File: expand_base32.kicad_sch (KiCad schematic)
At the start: 141 parts, among them J1 Vin, J10 LED_9, J11 LED_10, J12 H_5V, J13 S_5V, J14 H_3V3, J15 H_SERVO, J16 S_3V3, J17 BUZZER, J18 H_GND, J19 S_GND, J2 LED_1, J20 DIP_01, J21 INPUT DIP, J22 DIP_02, J23 LED_10, J24 LED_10, J25 DIP_01, J26 DIP_01, J27 INPUT_LM35, J28 POT_01, J29 POT_02, J3 LED_2, J30 LED_10, J31 INPUT_DS18B20, J32 LED_10, J33 LDR_01, J34 LED_10, J35 LED_10, J36 POT_02, J37 LED_10, J38 LED_10, J39 DIP_01, J4 LED_3, J40 DIP_01, J41 INPUT_BTN, J42 M1, J43 M2, J44 MOTOR SRC, J45 EN_1, J46 EN_2, J47 IN_M1A, J48 IN_M1B, J49 IN_M2A, J5 LED_4, J50 IN_M2B, J6 LED_5, J7 LED_6, J8 LED_7, J9 LED_8, M1 Servo, M2 Motor_DC, M3 Motor_DC, M4 MOTOR PAP, SW1 SW_DIP_x10, SW2 INPUT_D1, SW3 INPUT_D2, SW4 INPUT_D1, SW5 INPUT_D1, SW6 INPUT_D2, SW7 INPUT_D2, SW8 INPUT_D1, SW9 INPUT_D2, U1 LM7805_TO220, U2 L293D, U3 AMS1117, U4 ULN2003A, U6 DS18B20, U7 LM35-LP

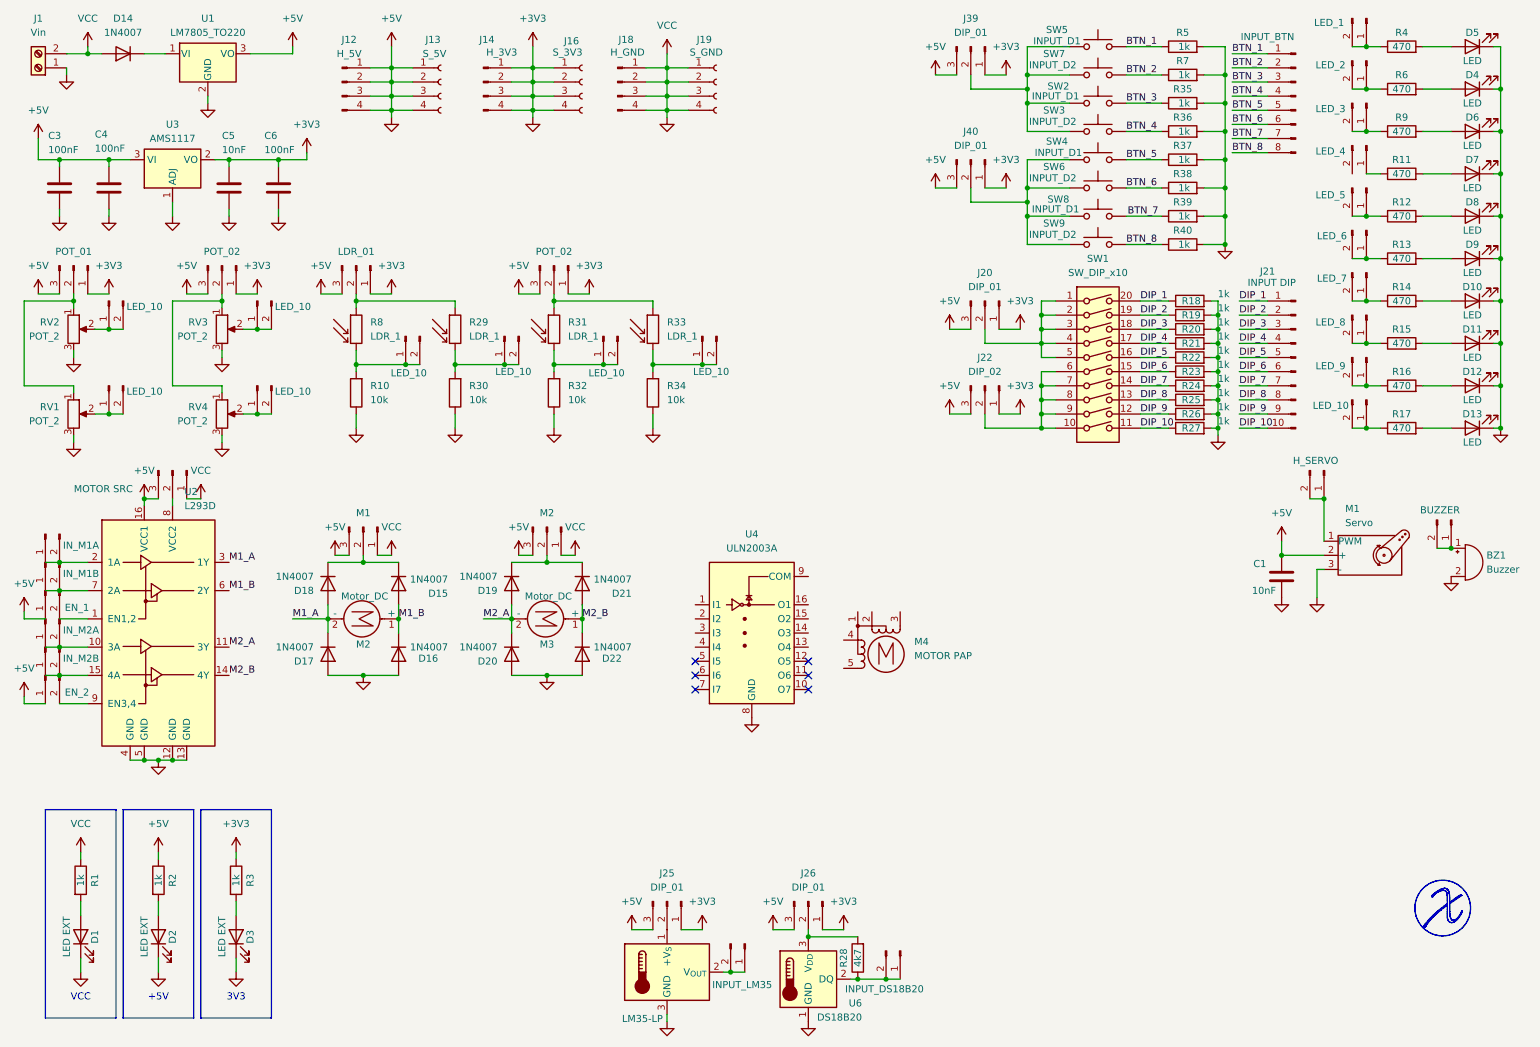
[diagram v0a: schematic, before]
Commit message: add: more components
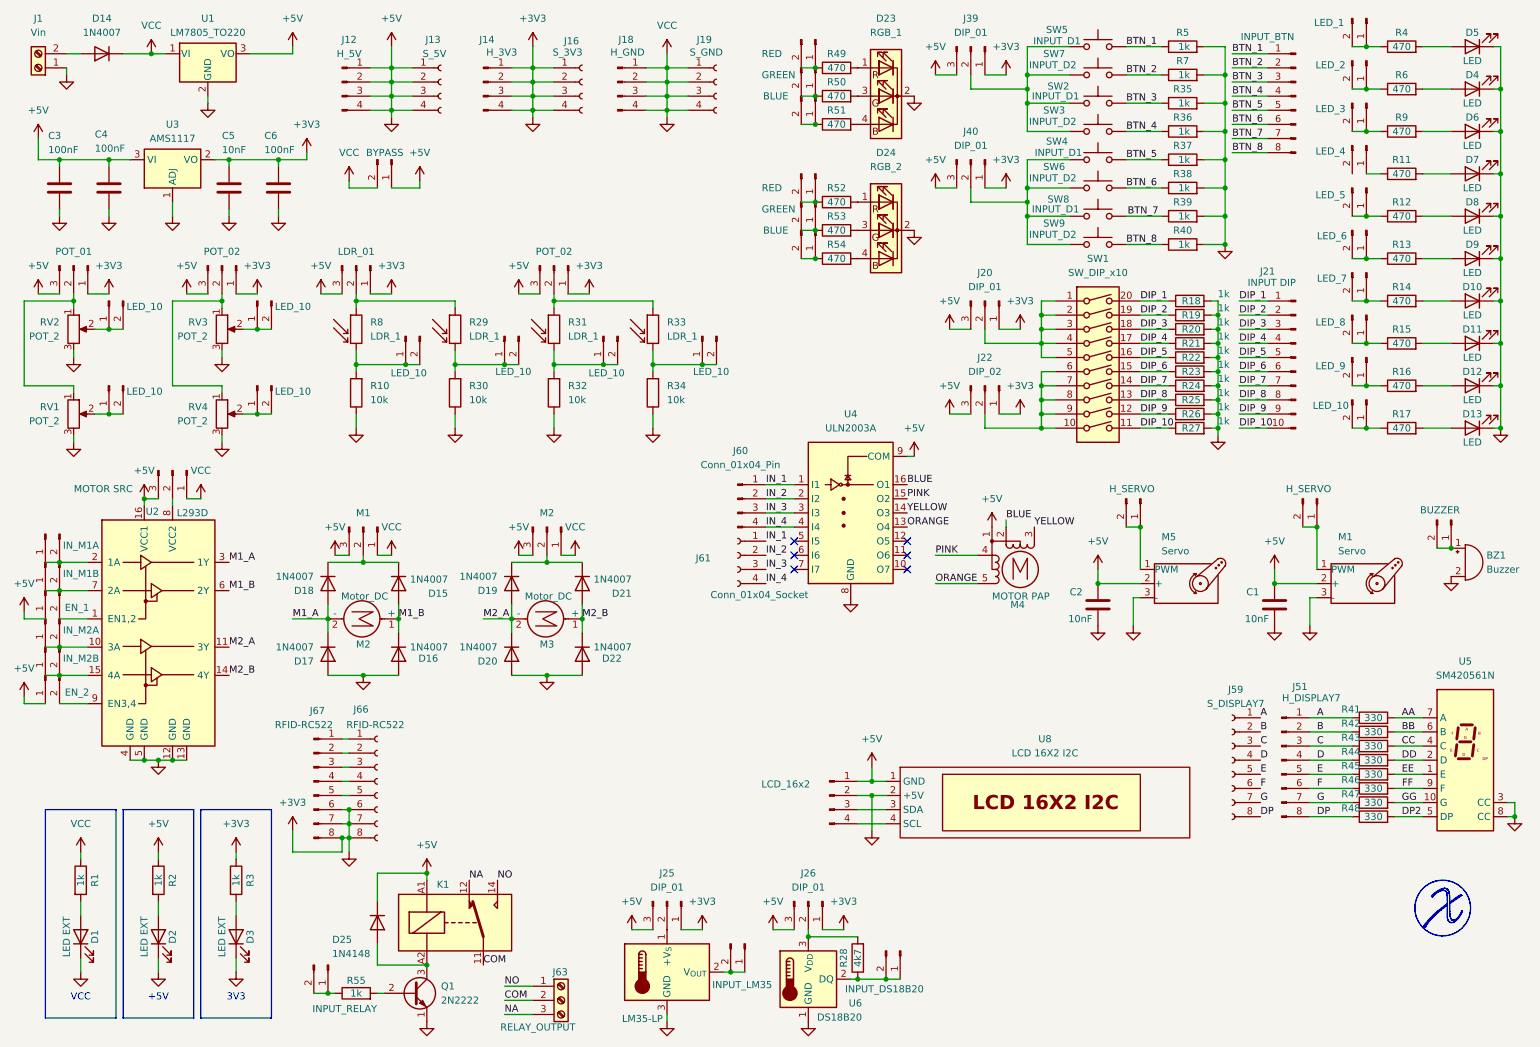
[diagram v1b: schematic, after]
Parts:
- added C2: 10nF, Capacitor_SMD:C_0805_2012Metric, symbol Device:C
- added D23: RGB_1, symbol Device:LED_RKGB
- added D24: RGB_2, symbol Device:LED_RKGB
- added D25: 1N4148, Diode_THT:D_DO-35_SOD27_P7.62mm_Horizontal, symbol Diode:1N4148
- added J51: H_DISPLAY7, Connector_PinHeader_2.54mm:PinHeader_1x08_P2.54mm_Vertical, symbol Connector:Conn_01x08_Pin
- added J52, J56: RED, Connector_PinHeader_2.54mm:PinHeader_1x02_P2.54mm_Vertical, symbol Connector:Conn_01x02_Pin
- added J53: BYPASS, Connector_PinHeader_2.54mm:PinHeader_1x02_P2.54mm_Vertical, symbol Connector:Conn_01x02_Pin
- added J54, J57: GREEN, Connector_PinHeader_2.54mm:PinHeader_1x02_P2.54mm_Vertical, symbol Connector:Conn_01x02_Pin
- added J55, J58: BLUE, Connector_PinHeader_2.54mm:PinHeader_1x02_P2.54mm_Vertical, symbol Connector:Conn_01x02_Pin
- added J59: S_DISPLAY7, symbol Connector:Conn_01x08_Socket
- added J60: Conn_01x04_Pin, symbol Connector:Conn_01x04_Pin
- added J61: Conn_01x04_Socket, symbol Connector:Conn_01x04_Socket
- added J62: H_SERVO, Connector_PinHeader_2.54mm:PinHeader_1x02_P2.54mm_Vertical, symbol Connector:Conn_01x02_Pin
- added J63: RELAY_OUTPUT, symbol Connector:Screw_Terminal_01x03
- added J64: LCD_16x2, symbol Connector:Conn_01x04_Pin
- added J65: INPUT_RELAY, Connector_PinHeader_2.54mm:PinHeader_1x02_P2.54mm_Vertical, symbol Connector:Conn_01x02_Pin
- added J66: RFID-RC522, symbol Connector:Conn_01x08_Socket
- added J67: RFID-RC522, symbol Connector:Conn_01x08_Pin
- added K1: JQC-3FF-005-1Z, Relay_THT:Relay_SPDT_Hongfa_JQC-3FF_0XX-1Z, symbol Relay:JQC-3FF-005-1Z
- added M5: Servo, Connector_PinHeader_2.54mm:PinHeader_1x03_P2.54mm_Vertical, symbol Motor:Motor_Servo_Futaba_J
- added Q1: 2N2222, Package_TO_SOT_THT:TO-92_Inline, symbol Transistor_BJT:PN2222A
- added R41, R42, R43, R44, R45, R46, R47, R48: 330, Resistor_THT:R_Axial_DIN0309_L9.0mm_D3.2mm_P12.70mm_Horizontal, symbol Device:R
- added R49, R50, R51, R52, R53, R54: 470, Resistor_THT:R_Axial_DIN0207_L6.3mm_D2.5mm_P10.16mm_Horizontal, symbol Device:R
- added R55: 1k, Resistor_THT:R_Axial_DIN0309_L9.0mm_D3.2mm_P12.70mm_Horizontal, symbol Device:R
- added U5: SM420561N, Display_7Segment:7SegmentLED_LTS6760_LTS6780, symbol Display_Character:SM420561N
- added U8: LCD 16X2 I2C, symbol lcd:LCD_I2C
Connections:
- net +3V3: now also D14.1 (K), M4.1, U1.1 (VI), U4.9 (COM), C2.1, C2.2, D23.2 (K), D24.2 (K), D25.1 (K), J53.1 (Pin_1), J53.2 (Pin_2), J64.1 (Pin_1), J64.2 (Pin_2), J66.6 (Pin_6), J66.7 (Pin_7), J66.8 (Pin_8), J67.6 (Pin_6), J67.7 (Pin_7), J67.8 (Pin_8), K1.A1, M5.2 (+), M5.3 (-), Q1.1 (E), U5.3 (CC), U5.8 (CC), U8.1 (GND), U8.2 (+5V); no longer D14.2 (A), J1.2 (Pin_2)
- net BLUE: now reaches M4.2
- net BLUE: now also U4.16 (O1)
- net YELLOW: now reaches M4.3 (-)
- net YELLOW: now also U4.14 (O3)
- net PINK: now reaches M4.4
- net PINK: now also U4.15 (O2)
- net ORANGE: now reaches M4.5
- net ORANGE: now also U4.13 (O4)
- net IN_1: now reaches U4.1 (I1)
- net IN_1: now also J60.1 (Pin_1), J61.1 (Pin_1)
- net IN_2: now reaches U4.2 (I2)
- net IN_2: now also J60.2 (Pin_2), J61.2 (Pin_2)
- net IN_3: now reaches U4.3 (I3)
- net IN_3: now also J60.3 (Pin_3), J61.3 (Pin_3)
- net IN_4: now reaches U4.4 (I4)
- net IN_4: now also J60.4 (Pin_4), J61.4 (Pin_4)
- new net: D25.2 (A), K1.A2, Q1.3 (C)
- new net: J52.1 (Pin_1), J52.2 (Pin_2), R49.1
- new net: J58.1 (Pin_1), J58.2 (Pin_2), R54.1
- new net: D24.4 (BA), R54.2
- new net: J66.1 (Pin_1), J67.1 (Pin_1)
- new net: J66.2 (Pin_2), J67.2 (Pin_2)
- new net: J66.3 (Pin_3), J67.3 (Pin_3)
- new net: J66.4 (Pin_4), J67.4 (Pin_4)
- new net: J66.5 (Pin_5), J67.5 (Pin_5)
- new net: J55.1 (Pin_1), J55.2 (Pin_2), R51.1
- new net: J65.1 (Pin_1), J65.2 (Pin_2), R55.1
- new net: D14.2 (A), J1.2 (Pin_2)
- new net: J64.3 (Pin_3), U8.3 (SDA)
- new net: J64.4 (Pin_4), U8.4 (SCL)
- new net: D24.1 (RA), R52.2
- new net: D24.3 (GA), R53.2
- new net: D23.1 (RA), R49.2
- new net: D23.3 (GA), R50.2
- new net: D23.4 (BA), R51.2
- new net: J56.1 (Pin_1), J56.2 (Pin_2), R52.1
- new net: J62.1 (Pin_1), J62.2 (Pin_2), M5.1 (PWM)
- new net: J54.1 (Pin_1), J54.2 (Pin_2), R50.1
- new net: J57.1 (Pin_1), J57.2 (Pin_2), R53.1
- new net: Q1.2 (B), R55.2
- new net A: J51.1 (Pin_1), J59.1 (Pin_1), R41.1
- new net AA: R41.2, U5.7 (A)
- new net B: J51.2 (Pin_2), J59.2 (Pin_2), R42.1
- new net BB: R42.2, U5.6 (B)
- new net C: J51.3 (Pin_3), J59.3 (Pin_3), R43.1
- new net CC: R43.2, U5.4 (C)
- new net COM: J63.2 (Pin_2), K1.11
- new net D: J51.4 (Pin_4), J59.4 (Pin_4), R44.1
- new net DD: R44.2, U5.2 (D)
- new net DP: J51.8 (Pin_8), J59.8 (Pin_8), R48.1
- new net DP2: R48.2, U5.5 (DP)
- new net E: J51.5 (Pin_5), J59.5 (Pin_5), R45.1
- new net EE: R45.2, U5.1 (E)
- new net F: J51.6 (Pin_6), J59.6 (Pin_6), R46.1
- new net FF: R46.2, U5.9 (F)
- new net G: J51.7 (Pin_7), J59.7 (Pin_7), R47.1
- new net GG: R47.2, U5.10 (G)
- new net NA: J63.3 (Pin_3), K1.12
- new net NO: J63.1 (Pin_1), K1.14
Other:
- company: (none) -> Xizuth Inc
- title: (none) -> Board Expantion base32
- moved on the sheet: C1, D14, M1, M4, U4

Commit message: add: footprints
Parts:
- added H1, H2, H3, H4: MountingHole_Pad, MountingHole:MountingHole_3mm_Pad, symbol Mechanical:MountingHole_Pad
- added J65, J67: DIP_01, Connector_PinHeader_2.54mm:PinHeader_1x03_P2.54mm_Vertical, symbol Connector:Conn_01x03_Pin
- added J69: INPUT_LM35, Connector_PinHeader_2.54mm:PinHeader_1x02_P2.54mm_Vertical, symbol Connector:Conn_01x02_Pin
- added J71: INPUT_DS18B20, Connector_PinHeader_2.54mm:PinHeader_1x02_P2.54mm_Vertical, symbol Connector:Conn_01x02_Pin
- added R56: 4k7, Resistor_THT:R_Axial_DIN0207_L6.3mm_D2.5mm_P10.16mm_Horizontal, symbol Device:R
- added U10: DS18B20, Package_TO_SOT_THT:TO-92_Inline, symbol Sensor_Temperature:DS18B20
- added U8: LM35-LP, Package_TO_SOT_THT:TO-92_Inline, symbol Sensor_Temperature:LM35-LP
- D4: renamed from D23; footprint (none) -> LED_THT:LED_D5.0mm-4_RGB
- D8: renamed from D24; footprint (none) -> LED_THT:LED_D5.0mm-4_RGB
- J14: renamed from J41; footprint (none) -> Connector_PinHeader_2.54mm:PinHeader_1x08_P2.54mm_Vertical
- J19: renamed from J40; footprint (none) -> Connector_PinHeader_2.54mm:PinHeader_1x03_P2.54mm_Vertical
- J25: renamed from J28; footprint (none) -> Connector_PinHeader_2.54mm:PinHeader_1x03_P2.54mm_Vertical
- J26: renamed from J29; footprint (none) -> Connector_PinHeader_2.54mm:PinHeader_1x03_P2.54mm_Vertical
- J27: renamed from J33; footprint (none) -> Connector_PinHeader_2.54mm:PinHeader_1x03_P2.54mm_Vertical
- J28: renamed from J36; footprint (none) -> Connector_PinHeader_2.54mm:PinHeader_1x03_P2.54mm_Vertical
- J3: renamed from J39; footprint (none) -> Connector_PinHeader_2.54mm:PinHeader_1x03_P2.54mm_Vertical
- J32: renamed from J20; footprint (none) -> Connector_PinHeader_2.54mm:PinHeader_1x03_P2.54mm_Vertical
- J38: renamed from J21; footprint (none) -> Connector_PinHeader_2.54mm:PinHeader_1x10_P2.54mm_Vertical
- J40: renamed from J67; value RFID-RC522 -> RFID-RC522_H; footprint (none) -> Connector_PinHeader_2.54mm:PinHeader_1x08_P2.54mm_Vertical
- J41: renamed from J66; value RFID-RC522 -> RFID-RC522_S; footprint (none) -> Connector_PinSocket_2.54mm:PinSocket_1x08_P2.54mm_Vertical
- J44: renamed from J22; footprint (none) -> Connector_PinSocket_2.54mm:PinSocket_1x03_P2.54mm_Vertical
- J46: renamed from J44; footprint (none) -> Connector_PinHeader_2.54mm:PinHeader_1x03_P2.54mm_Vertical
- J47: renamed from J42; footprint (none) -> Connector_PinHeader_2.54mm:PinHeader_1x03_P2.54mm_Vertical
- J5: renamed from J1; footprint (none) -> Connector_PinHeader_2.54mm:PinHeader_1x02_P2.54mm_Vertical
- J50: renamed from J64; footprint (none) -> Connector_PinSocket_2.54mm:PinSocket_1x04_P2.54mm_Vertical
- J55: renamed from J60; footprint (none) -> Connector_PinHeader_2.54mm:PinHeader_1x04_P2.54mm_Vertical
- J57: renamed from J43; footprint (none) -> Connector_PinHeader_2.54mm:PinHeader_1x03_P2.54mm_Vertical
- J59: renamed from J61; footprint (none) -> Connector_PinSocket_2.54mm:PinSocket_1x04_P2.54mm_Vertical
- J61: renamed from J59; footprint (none) -> Connector_PinHeader_2.54mm:PinHeader_1x08_P2.54mm_Vertical
- J63: footprint (none) -> TerminalBlock_Phoenix:TerminalBlock_Phoenix_MKDS-1,5-3_1x03_P5.00mm_Horizontal
- J64: renamed from J25; footprint (none) -> Connector_PinHeader_2.54mm:PinHeader_1x03_P2.54mm_Vertical
- J66: renamed from J26; footprint (none) -> Connector_PinHeader_2.54mm:PinHeader_1x03_P2.54mm_Vertical
- M1: renamed from M2; footprint (none) -> Connector_PinHeader_2.54mm:PinHeader_1x02_P2.54mm_Vertical
- M4: footprint (none) -> Connector_Molex:Molex_KK-254_AE-6410-05A_1x05_P2.54mm_Vertical
- M5: renamed from M3; footprint (none) -> Connector_PinHeader_2.54mm:PinHeader_1x02_P2.54mm_Vertical
- SW9: renamed from SW1; footprint (none) -> Button_Switch_THT:SW_DIP_SPSTx10_Slide_9.78x27.58mm_W7.62mm_P2.54mm
- U3: renamed from U8; footprint (none) -> Connector_PinSocket_2.54mm:PinSocket_1x04_P2.54mm_Vertical
- renumbered C3 to C1, C4 to C2, C5 to C3, C6 to C4, C2 to C5, C1 to C6, D5 to D1, D18 to D14, D17 to D16, D16 to D17, D25 to D18, D14 to D2, D21 to D20, D20 to D21, D1 to D23, D2 to D24, D3 to D25, D4 to D3, D6 to D5, D7 to D6, D8 to D7, J2 to J1, J16 to J10, J18 to J11, J19 to J12, J55 to J13, J4 to J15, J17 to J16, J5 to J17, J53 to J18, J52 to J2, J56 to J20, J6 to J21, J57 to J22, J58 to J23, J7 to J24, J8 to J29, J23 to J30, J30 to J31, J9 to J33, J37 to J36, J38 to J37, J10 to J39, J3 to J4, J24 to J42, J32 to J43, J11 to J45, J62 to J48, J15 to J49, J47 to J51, J48 to J52, J45 to J53, J49 to J54, J50 to J56, J46 to J58, J54 to J6, J65 to J60, J51 to J62, J27 to J68, J12 to J7, J31 to J70, J13 to J8, J14 to J9, M5 to M2, M1 to M3, R5 to R1, R9 to R10, R37 to R11, R11 to R12, R38 to R13, R52 to R14, R39 to R15, R12 to R16, R53 to R17, R40 to R18, R54 to R19, R4 to R2, R13 to R20, R18 to R21, R14 to R22, R19 to R23, R8 to R24, R29 to R25, R31 to R26, R33 to R27, R20 to R28, R21 to R29, R49 to R3, R15 to R30, R22 to R31, R23 to R32, R24 to R33, R16 to R34, R10 to R35, R30 to R36, R32 to R37, R34 to R38, R25 to R39, R7 to R4, R26 to R40, R27 to R41, R17 to R42, R41 to R43, R42 to R44, R43 to R45, R44 to R46, R45 to R47, R55 to R48, R46 to R49, R6 to R5, R47 to R50, R48 to R51, R1 to R52, R2 to R53, R3 to R54, R28 to R55, R50 to R6, R35 to R7, R51 to R8, R36 to R9, RV2 to RV1, RV3 to RV2, RV1 to RV3, SW5 to SW1, SW7 to SW2, SW2 to SW3, SW3 to SW4, SW4 to SW5, SW8 to SW7, SW9 to SW8, U3 to U2, U2 to U5, U5 to U6, U6 to U9
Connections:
- net +3V3: now also H1.1, H2.1, H3.1, H4.1, J65.1 (Pin_1), J65.3 (Pin_3), J67.1 (Pin_1), J67.3 (Pin_3), U10.1 (GND), U8.3 (GND)
- new net: J71.1 (Pin_1), J71.2 (Pin_2), R56.1, U10.2 (DQ)
- new net: J69.1 (Pin_1), J69.2 (Pin_2), U8.2 (V_{OUT})
- new net: J67.2 (Pin_2), R56.2, U10.3 (V_{DD})
- new net: J65.2 (Pin_2), U8.1 (+V_{S})
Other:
- moved on the sheet: BZ1, C5, C6, D14, D15, D16, D17, D18, D19, D20, D21, D22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
